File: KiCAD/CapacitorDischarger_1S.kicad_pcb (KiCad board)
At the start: 2 copper layers, 100 x 75 mm, 40 parts, among them J3 MKDS5/2-9.5, J4 MKDS5/2-9.5, J5 PM-128 input, Q1 MPSA42, Q2 STP10NK80Z

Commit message: Enclosure, front-panel LED via XH, DC-jack 9 V supply, build instructions
- mechanical/enclosure: parametric FreeCAD case for the single-sided board
  (base + screwed cover, PM-128 in the cover, sockets in line with J3/J4,
  9 V jack on the left wall with a floating-supply warning, LED on the front,
  baffled vents, snap hooks + supports for the 2-hole PCB), fit-check script
- LED1 off-board on a JST XH cable (J6); D_clamp2 (BZX55C8V2) holds LED_A at
  8.2 V if the LED is unplugged; sims 15/15 PASS; both boards re-placed, DRC clean
- PM-128 powered from any floating 9 V via a panel DC jack (battery box dropped)
- instruction.md: PCB making, assembly, wiring, tests, calibration, use

Co-Authored-By: Claude Opus 5.5 (1M context) <noreply@anthropic.com>
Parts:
- removed LED1: HLMP-4700 red, LED_THT:LED_D5.0mm
- added D_clamp2: BZX55C8V2, Diode_THT:D_DO-35_SOD27_P5.08mm_Vertical_AnodeUp, F.Cu at (139.0, 117.0)
- added J6: XH LED cable, Connector_JST:JST_XH_B2B-XH-A_1x02_P2.50mm_Vertical, F.Cu at (144.5, 120.0)
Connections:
- D_LED1 pad 2: Net-(D_LED1-A) -> /LED_A
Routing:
- net /LED_A: track 0.00 -> 10.4 mm
- net Net-(D_LED1-A): track 4.88 -> 0.00 mm

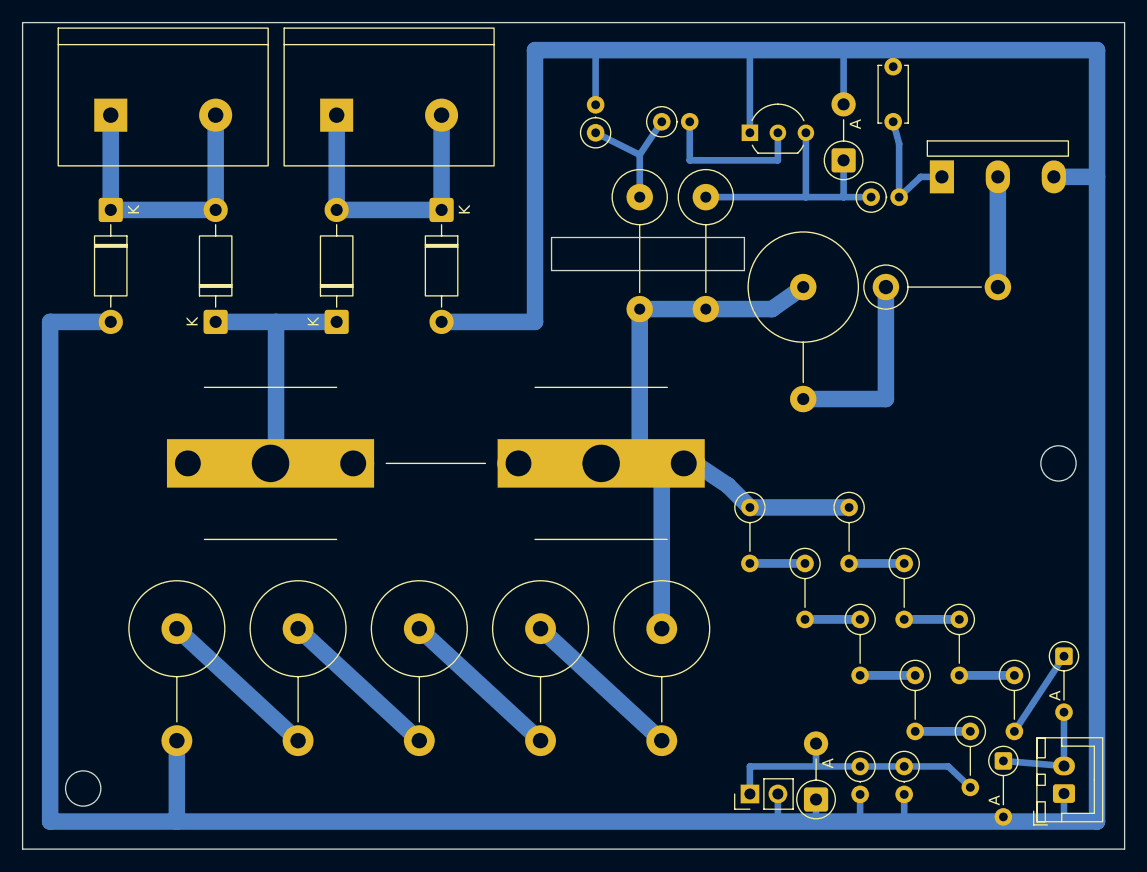
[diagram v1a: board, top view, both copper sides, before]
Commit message: 1S board for home etching: wider traces, GND pour, combined film sheets
- board_1s.py: tracks HV 2 mm / chains 1.2 mm / LV 1 mm; GND pour on B.Cu
  filled by kicad-cli with the voltage-aware rules (6 mm from HV, 0.4 mm
  from LV), so only ~40 % of the copper is etched; DRC clean
- gen_films.py: 1S_copper_components_1to1.pdf (B.Cu positive + mirrored
  F.Fab/F.SilkS for toner transfer) and 1S_solder_mask_1to1.pdf (2x B.Mask
  to stack), A4 portrait, images at the top; films and fab outputs regenerated
- instruction.md / PCB_info.md: toner-transfer steps, pour, new sheets

Co-Authored-By: Claude Opus 5.5 (1M context) <noreply@anthropic.com>
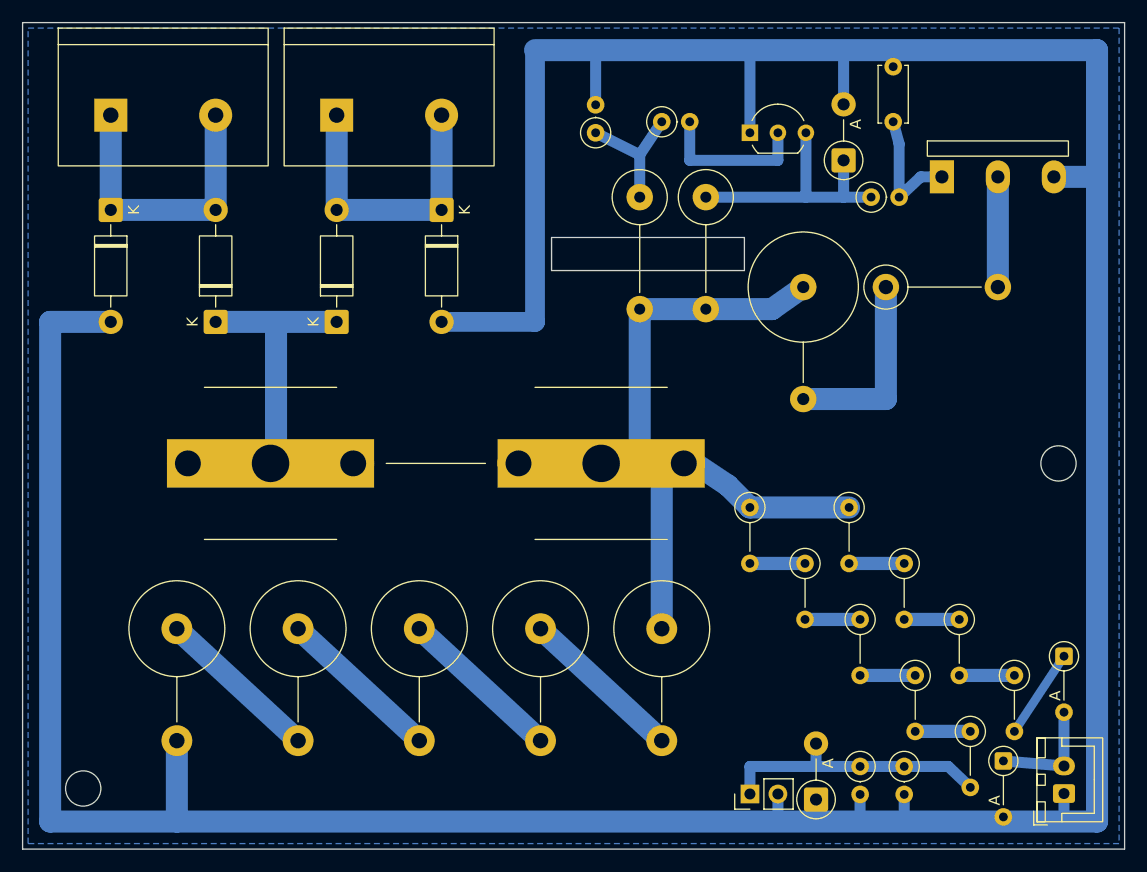
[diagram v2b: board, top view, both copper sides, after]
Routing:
- added copper zone on B.Cu, net /GND

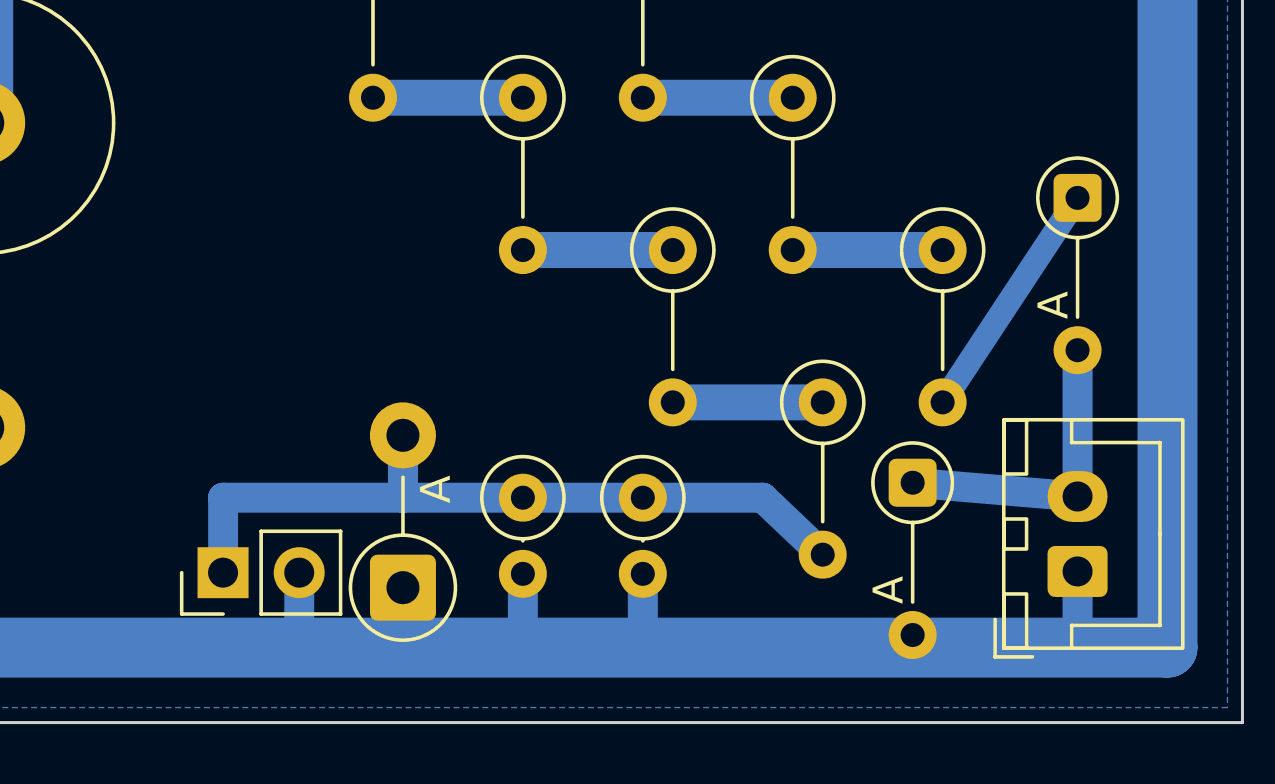
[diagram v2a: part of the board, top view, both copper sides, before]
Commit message: 1S board: 1 mm pour gaps for toner transfer, wider D_LED1-K link
- board_1s.py: GND pour keeps 1 mm from LV copper (was 0.4), 1 mm thermal
  gaps and 1 mm minimum neck, so toner no longer flakes around the gate
  drive (near Q2) and the J5/J6 corner
- J5 up 0.4 mm and its SIGOUT stub to y 67.0: 1 mm from the GND ring and
  from J5 pad 2
- D_LED1-K link 0.8 -> 1.2 mm with one bend, still 1.5 mm from R_LED4 pad 1
- DRC clean; only sub-1 mm gaps left are pad-to-pad inside 2.5/2.54 mm
  pitch footprints (0.80-0.94 mm)
- fab_1s outputs regenerated; PCB_info.md / instruction.md updated

Co-Authored-By: Claude Opus 5.5 <noreply@anthropic.com>
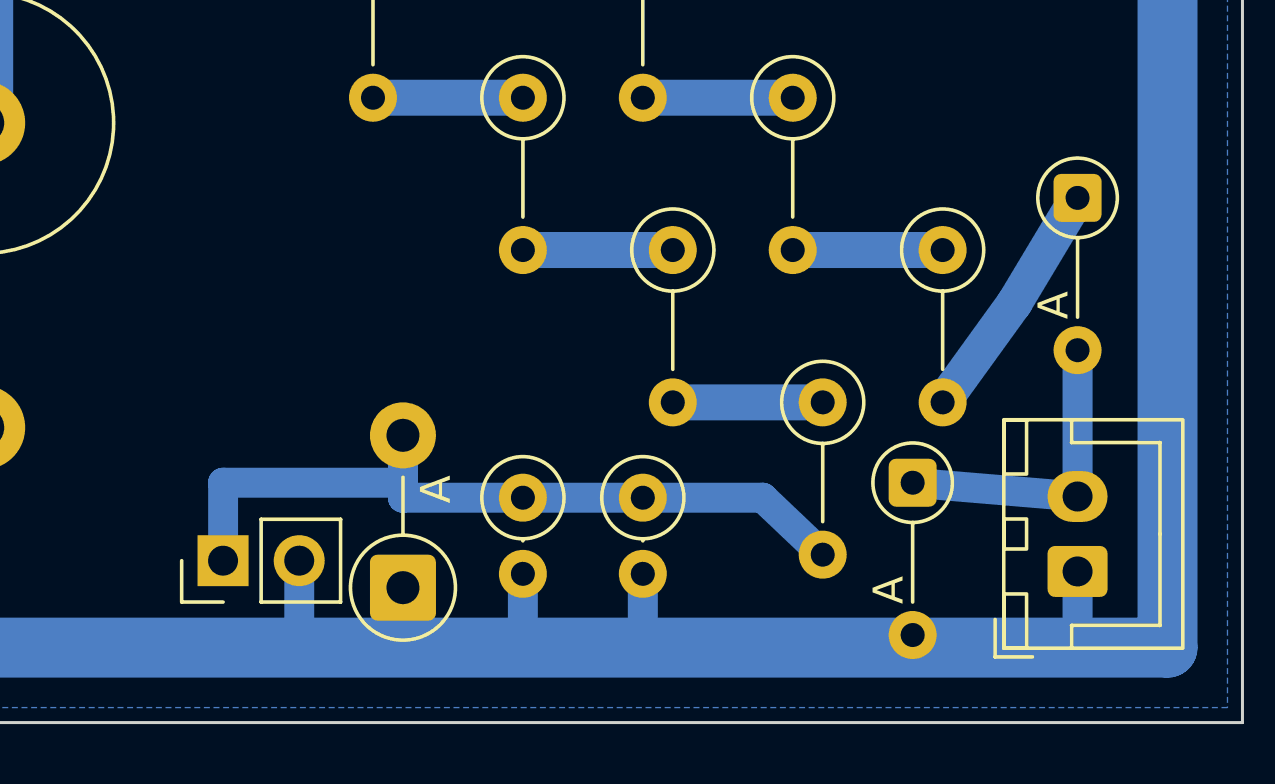
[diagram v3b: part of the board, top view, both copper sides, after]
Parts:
- moved J5 0.40 mm to (116.0, 119.6)
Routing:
- net /SIGOUT: track 25.3 -> 25.9 mm
